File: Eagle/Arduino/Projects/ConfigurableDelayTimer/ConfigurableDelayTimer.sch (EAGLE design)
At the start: 20 parts

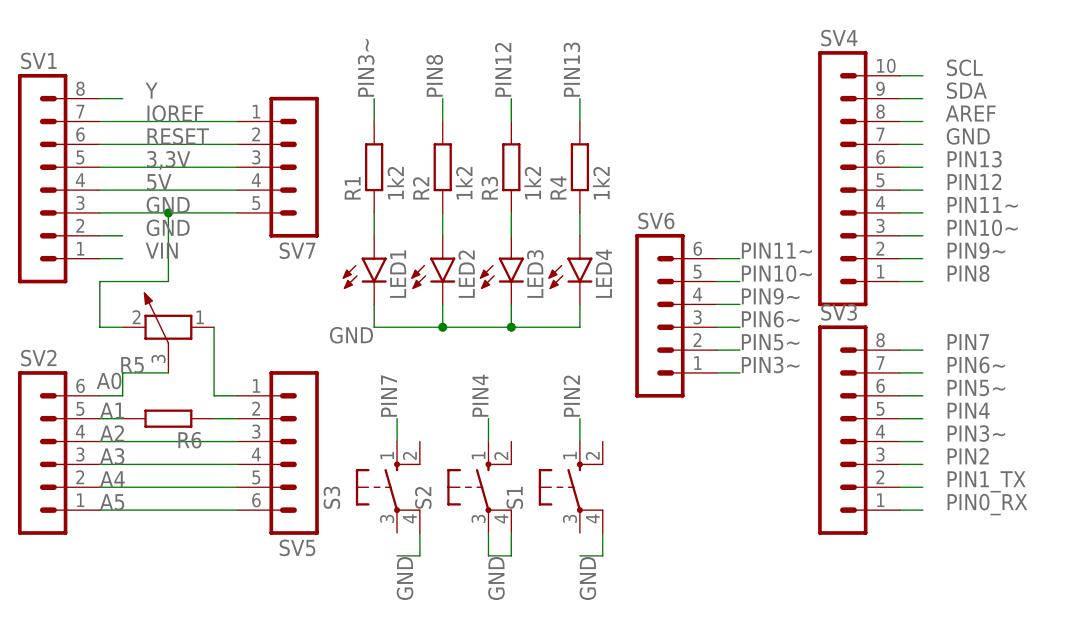
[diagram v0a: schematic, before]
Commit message: changed schematics - Measurement of current
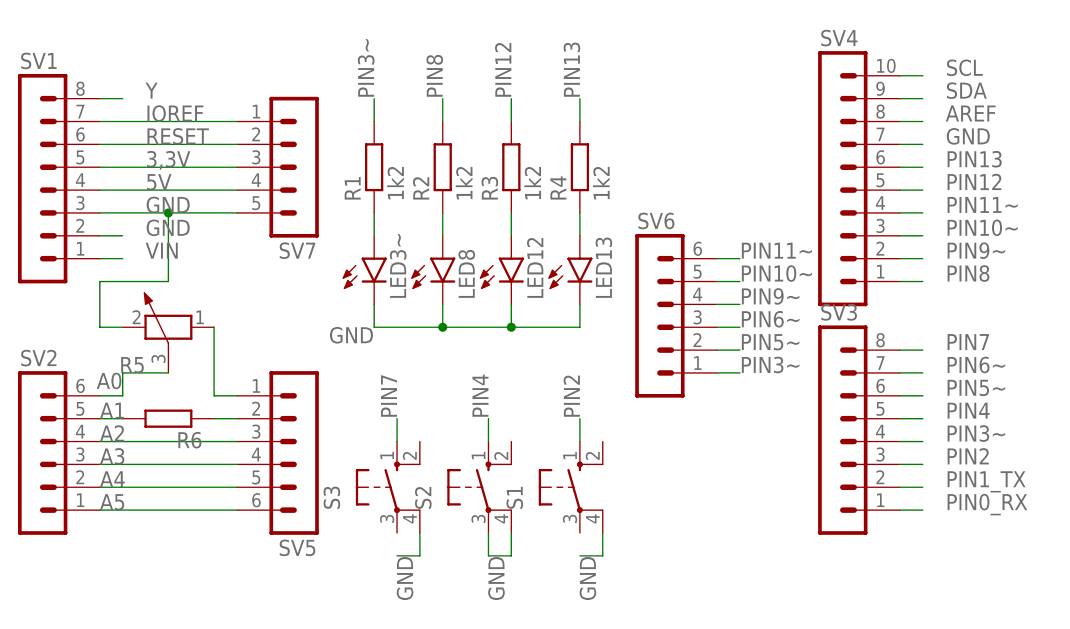
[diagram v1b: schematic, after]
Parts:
- renumbered LED1 to LED3~, LED2 to LED8, LED3 to LED12, LED4 to LED13
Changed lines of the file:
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@@
 <?xml version="1.0" encoding="utf-8"?>
 <!DOCTYPE eagle SYSTEM "eagle.dtd">
-<eagle version="9.3.2">
+<eagle version="9.6.2">
 <drawing>
 <settings>
@@
 <part name="S2" library="switch-omron" library_urn="urn:adsk.eagle:library:377" deviceset="40-XX" device="" package3d_urn="urn:adsk.eagle:package:27483/1"/>
 <part name="S3" library="switch-omron" library_urn="urn:adsk.eagle:library:377" deviceset="40-XX" device="" package3d_urn="urn:adsk.eagle:package:27483/1"/>
-<part name="LED1" library="led" library_urn="urn:adsk.eagle:library:259" deviceset="LED" device="5MM" package3d_urn="urn:adsk.eagle:package:15799/2"/>
-<part name="LED2" library="led" library_urn="urn:adsk.eagle:library:259" deviceset="LED" device="5MM" package3d_urn="urn:adsk.eagle:package:15799/2"/>
-<part name="LED3" library="led" library_urn="urn:adsk.eagle:library:259" deviceset="LED" device="5MM" package3d_urn="urn:adsk.eagle:package:15799/2"/>
-<part name="LED4" library="led" library_urn="urn:adsk.eagle:library:259" deviceset="LED" device="5MM" package3d_urn="urn:adsk.eagle:package:15799/2"/>
+<part name="LED3~" library="led" library_urn="urn:adsk.eagle:library:259" deviceset="LED" device="5MM" package3d_urn="urn:adsk.eagle:package:15799/2"/>
+<part name="LED8" library="led" library_urn="urn:adsk.eagle:library:259" deviceset="LED" device="5MM" package3d_urn="urn:adsk.eagle:package:15799/2"/>
+<part name="LED12" library="led" library_urn="urn:adsk.eagle:library:259" deviceset="LED" device="5MM" package3d_urn="urn:adsk.eagle:package:15799/2"/>
+<part name="LED13" library="led" library_urn="urn:adsk.eagle:library:259" deviceset="LED" device="5MM" package3d_urn="urn:adsk.eagle:package:15799/2"/>
 <part name="R1" library="rcl" library_urn="urn:adsk.eagle:library:334" deviceset="R-EU_" device="0207/7" package3d_urn="urn:adsk.eagle:package:23493/2" value="1k2"/>
 <part name="R2" library="rcl" library_urn="urn:adsk.eagle:library:334" deviceset="R-EU_" device="0207/7" package3d_urn="urn:adsk.eagle:package:23493/2" value="1k2"/>
@@
 <attribute name="VALUE" x="52.07" y="64.135" size="1.778" layer="96" rot="R90"/>
 </instance>
-<instance part="LED1" gate="G$1" x="53.34" y="86.36" smashed="yes">
+<instance part="LED3~" gate="G$1" x="53.34" y="86.36" smashed="yes">
 <attribute name="NAME" x="56.896" y="81.788" size="1.778" layer="95" rot="R90"/>
 <attribute name="VALUE" x="59.055" y="81.788" size="1.778" layer="96" rot="R90"/>
 </instance>
-<instance part="LED2" gate="G$1" x="60.96" y="86.36" smashed="yes">
+<instance part="LED8" gate="G$1" x="60.96" y="86.36" smashed="yes">
 <attribute name="NAME" x="64.516" y="81.788" size="1.778" layer="95" rot="R90"/>
 <attribute name="VALUE" x="66.675" y="81.788" size="1.778" layer="96" rot="R90"/>
 </instance>
-<instance part="LED3" gate="G$1" x="68.58" y="86.36" smashed="yes">
+<instance part="LED12" gate="G$1" x="68.58" y="86.36" smashed="yes">
 <attribute name="NAME" x="72.136" y="81.788" size="1.778" layer="95" rot="R90"/>
 <attribute name="VALUE" x="74.295" y="81.788" size="1.778" layer="96" rot="R90"/>
 </instance>
-<instance part="LED4" gate="G$1" x="76.2" y="86.36" smashed="yes">
+<instance part="LED13" gate="G$1" x="76.2" y="86.36" smashed="yes">
 <attribute name="NAME" x="79.756" y="81.788" size="1.778" layer="95" rot="R90"/>
 <attribute name="VALUE" x="81.915" y="81.788" size="1.778" layer="96" rot="R90"/>
@@
 </segment>
 <segment>
-<pinref part="LED1" gate="G$1" pin="C"/>
+<pinref part="LED3~" gate="G$1" pin="C"/>
 <wire x1="53.34" y1="81.28" x2="53.34" y2="78.74" width="0.1524" layer="91"/>
 <wire x1="53.34" y1="78.74" x2="60.96" y2="78.74" width="0.1524" layer="91"/>
-<pinref part="LED2" gate="G$1" pin="C"/>
+<pinref part="LED8" gate="G$1" pin="C"/>
 <wire x1="60.96" y1="78.74" x2="60.96" y2="81.28" width="0.1524" layer="91"/>
-<pinref part="LED3" gate="G$1" pin="C"/>
+<pinref part="LED12" gate="G$1" pin="C"/>
 <wire x1="60.96" y1="78.74" x2="68.58" y2="78.74" width="0.1524" layer="91"/>
 <wire x1="68.58" y1="78.74" x2="68.58" y2="81.28" width="0.1524" layer="91"/>
 <junction x="60.96" y="78.74"/>
-<pinref part="LED4" gate="G$1" pin="C"/>
+<pinref part="LED13" gate="G$1" pin="C"/>
 <wire x1="68.58" y1="78.74" x2="76.2" y2="78.74" width="0.1524" layer="91"/>
 <wire x1="76.2" y1="78.74" x2="76.2" y2="81.28" width="0.1524" layer="91"/>
@@
 <segment>
 <pinref part="R1" gate="G$1" pin="1"/>
-<pinref part="LED1" gate="G$1" pin="A"/>
+<pinref part="LED3~" gate="G$1" pin="A"/>
 <wire x1="53.34" y1="91.44" x2="53.34" y2="88.9" width="0.1524" layer="91"/>
 </segment>
@@
 <segment>
 <pinref part="R2" gate="G$1" pin="1"/>
-<pinref part="LED2" gate="G$1" pin="A"/>
+<pinref part="LED8" gate="G$1" pin="A"/>
 <wire x1="60.96" y1="91.44" x2="60.96" y2="88.9" width="0.1524" layer="91"/>
 </segment>
@@
 <segment>
 <pinref part="R3" gate="G$1" pin="1"/>
-<pinref part="LED3" gate="G$1" pin="A"/>
+<pinref part="LED12" gate="G$1" pin="A"/>
 <wire x1="68.58" y1="91.44" x2="68.58" y2="88.9" width="0.1524" layer="91"/>
 </segment>
@@
 <segment>
 <pinref part="R4" gate="G$1" pin="1"/>
-<pinref part="LED4" gate="G$1" pin="A"/>
+<pinref part="LED13" gate="G$1" pin="A"/>
 <wire x1="76.2" y1="91.44" x2="76.2" y2="88.9" width="0.1524" layer="91"/>
 </segment>
